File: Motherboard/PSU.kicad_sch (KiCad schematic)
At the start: 113 parts, among them J18 USB_C_Receptacle_USB2.0, J85 JST_XHP2_Battery1, J86 JST_XHP2_Battery2, J87 JST_XHP2_Battery3, J88 JST_XHP2_Battery4, J89 JST_XHP2_Battery5, Q78 CSD17303Q5, Q79 CSD17303Q5, Q8 2N7002, SW1 SW_Push, SW2 SW_Push, U14 CH224K, U15 SY8253ADC, U16 SY8253ADC, U79 BQ25798, U81 TPS61088RHLR, U82 BQ27441DRZT-G1A

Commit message: Added RP2040 MCU, Handles all External IO Systems (Except Audio), WIP.
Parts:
- removed SW1: SW_Push, easyeda2kicad:SW-TH_TM-007-D1-A-03, symbol Switch:SW_Push
- added D23, D28: SS54, A_HDJ_Library:D_SMA, symbol Device:D_Schottky
- added Q80: 2N7002, Package_TO_SOT_SMD:SOT-23, symbol Transistor_FET:2N7002
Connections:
- net BAT+: now also D28.1 (K); no longer C137.2, J85.1 (Pin_1), J86.1 (Pin_1), J87.1 (Pin_1), J88.1 (Pin_1), J89.1 (Pin_1), R93.2, U82.6 (BAT), U82.8 (SRP)
- net GND: now also Q80.2 (S)
- net PWR: now also Q80.3 (D)
- net VDC: now also D23.1 (K); no longer C106.2, C107.2, C108.2, R79.2, U81.14 (VOUT), U81.15 (VOUT), U81.16 (VOUT)
- new net: C106.2, C107.2, C108.2, D23.2 (A), R79.2, U81.14 (VOUT), U81.15 (VOUT), U81.16 (VOUT)
- new net: C137.2, D28.2 (A), J85.1 (Pin_1), J86.1 (Pin_1), J87.1 (Pin_1), J88.1 (Pin_1), J89.1 (Pin_1), R93.2, U82.6 (BAT), U82.8 (SRP)
- new net PWR_Button: Q80.1 (G)
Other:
- moved on the sheet: C69, D25, R55, R56, SW2

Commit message: Added stereo Audio using CP2615 > PCM5102A > PAM8403D through USB (Mu has dysfunctional I2S)
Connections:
- net STAT_LED renamed BAT_STAT
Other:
- note added: "15V PD Input"
- note added: "CH224K get DC 9-20V power from USB-PD adapter"
- note removed: "12V PD Input"
- note removed: "CH224K get DC 9-20V (12V) power from USB-PD adapter"
- moved on the sheet: C100, C102, C103, C104, C105, C106, C107, C108, C109, C131, C132, C133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

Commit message: Motherboard Complete (aside from parts-BOM associations)
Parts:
- removed J18: USB_C_Receptacle_USB2.0, A_HDJ_Library:USB_C_Receptacle_G-Switch_GT-USB-7010ASV, symbol Connector:USB_C_Receptacle_USB2.0_16P
- removed Q8: 2N7002, A_HDJ_Library:SOT-23, symbol Transistor_FET:2N7002
- added C162: 100pF, A_HDJ_Library:C_0603_1608Metric, symbol Device:C
- added C163: 1.8nF, A_HDJ_Library:C_0603_1608Metric, symbol Device:C
- added C88: 10uF/25V, A_HDJ_Library:C_0603_1608Metric, symbol Device:C
- added C89: 100nF/25V, A_HDJ_Library:C_0603_1608Metric, symbol Device:C
- added C91: 220pF/50V, A_HDJ_Library:C_0603_1608Metric, symbol Device:C
- added C98: 22uF/10V, A_HDJ_Library:C_0603_1608Metric, symbol Device:C
- added J80: USB_C_Receptacle_USB2.0_16P, symbol Connector:USB_C_Receptacle_USB2.0_16P
- added L3: 2.2uH/9.2A, A_HDJ_Library:L_Sunlord_SWPA4020S, symbol Device:L
- added Q81: 2N7002, Package_TO_SOT_SMD:SOT-23, symbol Transistor_FET:2N7002
- added R96: 23.7k/1%, A_HDJ_Library:R_0402_1005Metric, symbol Device:R
- added R99: 100K/1%, A_HDJ_Library:R_0402_1005Metric, symbol Device:R
- added U86: TPS62131, Package_DFN_QFN:VQFN-16-1EP_3x3mm_P0.5mm_EP1.68x1.68mm_ThermalVias, symbol Regulator_Switching:TPS62131
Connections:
- net +15V: now also J80.A4 (VBUS), J80.A9 (VBUS), J80.B4 (VBUS), J80.B9 (VBUS)
- net CC1: now also J80.A5 (CC1)
- net CC2: now also J80.B5 (CC2)
- net GND: now also U82.13 (PAD), C162.2, C88.1, C89.1, C91.1, C98.1, J80.A1 (GND), J80.A12 (GND), J80.B1 (GND), J80.B12 (GND), J80.SH (SHIELD), Q81.2 (S), R96.1, U86.15 (GND), U86.16 (GND), U86.17 (GND), U86.5 (FB), U86.6 (GND), U86.8 (DEF)
- net PWR_C_D+: now also J80.A6 (D+), J80.B6 (D+)
- net PWR_C_D-: now also J80.A7 (D-), J80.B7 (D-)
- net VDC: now also C88.2, C89.2, U86.10 (VIN), U86.11 (VIN), U86.12 (VIN), U86.13 (EN)
- net at R47.2, R49.2: now also Q81.1 (G)
- net at U81.18 (COMP): now also C162.1, C163.1
- net at D22.1 (K): now also Q81.3 (D)
- new net: L3.1, U86.1 (SW), U86.2 (SW), U86.3 (SW)
- new net: R99.2, U86.4 (PG)
- new net: C91.2, U86.9 (SS/TR)
- new net: C163.2, R96.2
- new net +1V8: C98.2, L3.2, R99.1, U86.14 (VOS), U86.7 (FSW)
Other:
- moved on the sheet: C66, C69, D21, D25, Q80, R46, R48, R50, R55, R56, SW2

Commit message: Quick Save
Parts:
- J80: footprint (none) -> Connector_USB:USB_C_Receptacle_GCT_USB4105-xx-A_16P_TopMnt_Horizontal
- U81: footprint RHL0020A -> TPS61088:RHL0020A
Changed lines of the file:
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@@
 			)
 		)
-		(property "Footprint" ""
+		(property "Footprint" "Connector_USB:USB_C_Receptacle_GCT_USB4105-xx-A_16P_TopMnt_Horizontal"
 			(at 124.46 260.35 0)
 			(hide yes)
@@
 			)
 		)
-		(property "Footprint" "RHL0020A"
+		(property "Footprint" "TPS61088:RHL0020A"
 			(at 292.608 179.07 0)
 			(hide yes)

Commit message: Switched Screens to use RGB interface, ADV7613 -> ADV7611. Changes WIP
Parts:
- removed R61, R62: 10K/1%, A_HDJ_Library:R_0402_1005Metric, symbol Device:R
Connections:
- no-connect marks 8 -> 10

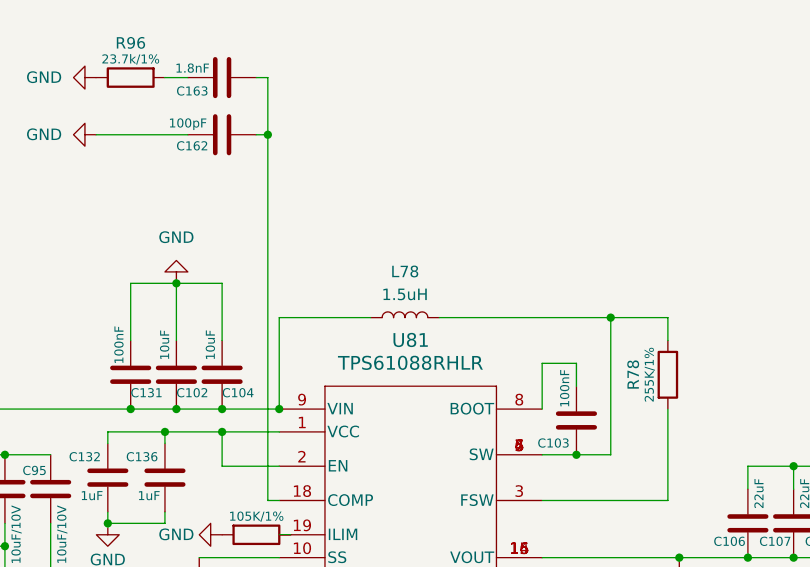
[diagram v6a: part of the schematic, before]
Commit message: Partial wiring of power path and top screen
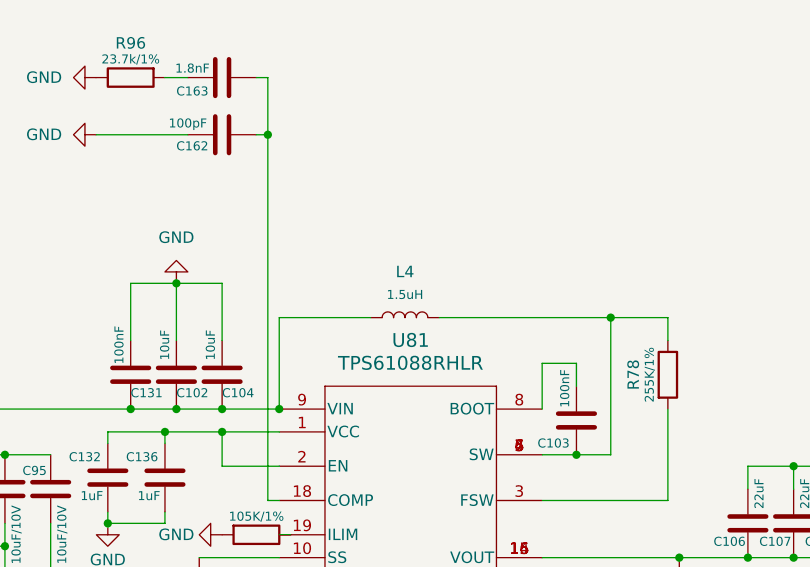
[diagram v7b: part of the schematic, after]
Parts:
- removed L78: 1.5uH, symbol Device:L
- added L4: 1.5uH, A_HDJ_Library:L_Sunlord_SWPA4020S, symbol Device:L
- TH78: footprint (none) -> A_HDJ_Library:R_0603_1608Metric
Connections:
- net at C103.2, R78.1, U81.4 (SW)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: now also L4.2
- net at C102.2, C104.2, C131.2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: now also L4.1
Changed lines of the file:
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@@
 			)
 		)
-		(property "Footprint" ""
+		(property "Footprint" "A_HDJ_Library:R_0603_1608Metric"
 			(at 190.5 177.8 0)
 			(hide yes)
@@
 	)
 	(symbol
-		(lib_id "Device:L")
-		(at 292.1 152.4 90)
-		(unit 1)
-		(body_style 1)
-		(exclude_from_sim no)
-		(in_bom yes)
-		(on_board yes)
-		(in_pos_files yes)
-		(dnp no)
-		(fields_autoplaced yes)
-		(property "Reference" "L78"
-			(at 292.1 147.32 90)
-			(show_name no)
-			(do_not_autoplace no)
-			(effects
-				(font
-					(size 1.27 1.27)
-				)
-			)
-		)
-		(property "Value" "1.5uH"
-			(at 292.1 149.86 90)
-			(show_name no)
-			(do_not_autoplace no)
-			(effects
-				(font
-					(size 1.27 1.27)
-				)
-			)
-		)
-		(property "Footprint" ""
-			(at 292.1 152.4 0)
-			(hide yes)
-			(show_name no)
-			(do_not_autoplace no)
-			(effects
-				(font
-					(size 1.27 1.27)
-				)
-			)
-		)
-		(property "Datasheet" ""
-			(at 292.1 152.4 0)
-			(hide yes)
-			(show_name no)
-			(do_not_autoplace no)
-			(effects
-				(font
-					(size 1.27 1.27)
-				)
-			)
-		)
-		(property "Description" "Inductor"
-			(at 292.1 152.4 0)
-			(hide yes)
-			(show_name no)
-			(do_not_autoplace no)
-			(effects
-				(font
-					(size 1.27 1.27)
-				)
-			)
-		)
-		(pin "1"
-		)
-		(pin "2"
-		)
-		(instances
-			(project "Motherboard"
-				(path "/2a6d114a-7fd7-4207-b5f7-4ea9c34f36aa/b23aee49-27d1-466d-98e2-113ee657e42b"
-					(reference "L78")
-					(unit 1)
-				)
-			)
-		)
-	)
-	(symbol
 		(lib_id "power:+5V")
 		(at 478.79 179.07 0)
@@
 					(unit 1)
 				)
+			)
+		)
+	)
+	(symbol
+		(lib_id "Device:L")
+		(at 292.1 152.4 90)
+		(unit 1)
+		(body_style 1)
+		(exclude_from_sim no)
+		(in_bom yes)
+		(on_board yes)
+		(in_pos_files yes)
+		(dnp no)
+		(fields_autoplaced yes)
+		(property "Reference" "L4"
+			(at 292.1 147.32 90)
+			(show_name no)
+			(do_not_autoplace no)
+			(effects
+				(font
+					(size 1.27 1.27)
+				)
+			)
+		)
+		(property "Value" "1.5uH"
+			(at 292.1 149.86 90)
+			(show_name no)
+			(do_not_autoplace no)
+			(effects
+				(font
+					(size 1 1)
+				)
+			)
+		)
+		(property "Footprint" "A_HDJ_Library:L_Sunlord_SWPA4020S"
+			(at 292.1 152.4 0)
+			(hide yes)
+			(show_name no)
+			(do_not_autoplace no)
+			(effects
+				(font
+					(size 1.27 1.27)
+				)
+			)
+		)
+		(property "Datasheet" ""
+			(at 292.1 152.4 0)
+			(hide yes)
+			(show_name no)
+			(do_not_autoplace no)
+			(effects
+				(font
+					(size 1.27 1.27)
+				)
+			)
+		)
+		(property "Description" ""
+			(at 292.1 152.4 0)
+			(hide yes)
+			(show_name no)
+			(do_not_autoplace no)
+			(effects
+				(font
+					(size 1.27 1.27)
+				)
+			)
+		)
+		(property "SCH_Show_Footprint" ""
+			(at 292.1 152.4 0)
+			(hide yes)
+			(show_name no)
+			(do_not_autoplace no)
+			(effects
+				(font
+					(size 1.27 1.27)
+				)
+			)
+		)
+		(property "Sim.Device" ""
+			(at 292.1 152.4 0)
+			(hide yes)
+			(show_name no)
+			(do_not_autoplace no)
+			(effects
+				(font
+					(size 1.27 1.27)
+				)
+			)
+		)
+		(property "Sim.Pins" ""
+			(at 292.1 152.4 0)
+			(hide yes)
+			(show_name no)
+			(do_not_autoplace no)
+			(effects
+				(font
+					(size 1.27 1.27)
+				)
+			)
+		)
+		(property "Sim.Type" ""
+			(at 292.1 152.4 0)
+			(hide yes)
+			(show_name no)
+			(do_not_autoplace no)
+			(effects
+				(font
+					(size 1.27 1.27)
+				)
+			)
+		)
+		(property "Buy_Link" ""
+			(at 455.93 567.69 0)
+			(hide yes)
+			(show_name no)
+			(do_not_autoplace no)
+			(effects
+				(font
+					(size 1.27 1.27)
+				)
+			)
+		)
+		(property "DF_Comment" "贴片屏蔽电感2.2uH_4.0*4.0*2.0_4.3A"
+			(at 455.93 567.69 0)
+			(hide yes)
+			(show_name no)
+			(do_not_autoplace no)
+			(effects
+				(font
+					(size 1.27 1.27)
+				)
+			)
+		)
+		(property "Field-1" ""
+			(at 455.93 567.69 0)
+			(hide yes)
+			(show_name no)
+			(do_not_autoplace no)
+			(effects
+				(font
+					(size 1.27 1.27)
+				)
+			)
+		)
+		(pin "1"
+		)
+		(pin "2"
+		)
+		(instances
+			(project "Motherboard"
+				(path "/2a6d114a-7fd7-4207-b5f7-4ea9c34f36aa/b23aee49-27d1-466d-98e2-113ee657e42b"
+					(reference "L4")
+					(unit 1)
+				)

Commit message: Wired PSU (May need to be edited, Screen connector location needs to be verified)
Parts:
- R76: footprint A_HDJ_Library:R_0402_1005Metric -> Resistor_SMD:R_1206_3216Metric
- R78, R79, R87, R96: footprint A_HDJ_Library:R_0402_1005Metric -> A_HDJ_Library:R_0805_2012Metric
- R91: footprint A_HDJ_Library:R_0402_1005Metric -> A_HDJ_Library:R_0603_1608Metric
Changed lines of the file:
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@@
 			)
 		)
-		(property "Footprint" "A_HDJ_Library:R_0402_1005Metric"
+		(property "Footprint" "A_HDJ_Library:R_0805_2012Metric"
 			(at 320.802 190.5 90)
 			(hide yes)
@@
 			)
 		)
-		(property "Footprint" "A_HDJ_Library:R_0402_1005Metric"
+		(property "Footprint" "A_HDJ_Library:R_0805_2012Metric"
 			(at 319.532 158.75 90)
 			(hide yes)
@@
 			)
 		)
-		(property "Footprint" "A_HDJ_Library:R_0402_1005Metric"
+		(property "Footprint" "Resistor_SMD:R_1206_3216Metric"
 			(at 231.14 179.578 90)
 			(hide yes)
@@
 			)
 		)
-		(property "Footprint" "A_HDJ_Library:R_0402_1005Metric"
+		(property "Footprint" "A_HDJ_Library:R_0805_2012Metric"
 			(at 320.802 182.88 90)
 			(hide yes)
@@
 			)
 		)
-		(property "Footprint" "A_HDJ_Library:R_0402_1005Metric"
+		(property "Footprint" "A_HDJ_Library:R_0603_1608Metric"
 			(at 275.082 237.49 90)
 			(hide yes)
@@
 			)
 		)
-		(property "Footprint" "A_HDJ_Library:R_0402_1005Metric"
+		(property "Footprint" "A_HDJ_Library:R_0805_2012Metric"
 			(at 261.62 123.952 90)
 			(hide yes)
